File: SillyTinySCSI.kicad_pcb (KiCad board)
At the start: 4 copper layers, 53.5 x 25 mm, 53 parts, among them J301 Micro_SD_Card_Det1, J302 DB25_Plug, U1 Pico W, U101 74LVT125, U102 74LVT125, U105 74LVT245, U106 74LVT245, U301 MIC5219-2.85YM5

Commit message: fix BOM and proposed RTM files
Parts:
- added D304: LED, LED_SMD:LED_0805_2012Metric, F.Cu at (159.3, 51.7)
- R304: value 62 -> 51
- RN301, RN302: value 110 -> 120
- moved D302 0.32 mm to (159.3, 51.7)
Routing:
- net GND: track 110.3 -> 119.1 mm, vias 21 -> 24
- net Net-(D302-A): track 1.61 -> 9.69 mm, vias 0 -> 1
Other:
- board text added: "ZuluSCSI OSHW derivative by"
- board text removed: "${Brand} Pico OSHW derivative by"

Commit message: routing improvements
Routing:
- net +3V0: track 186.6 -> 199.2 mm
- net /cpu/SDIO_CLK: track 51.5 -> 47.1 mm
- net GND: track 119.1 -> 114.7 mm, vias 24 -> 25
- net /cpu/SDIO_D1: track 68.0 -> 63.8 mm
- net /cpu/SDIO_D3: track 66.7 -> 64.8 mm
- net /cpu/SDIO_D2: track 65.3 -> 63.4 mm
- net /cpu/SDIO_D0: track 61.0 -> 60.2 mm
- net +5V: track 59.5 -> 60.0 mm

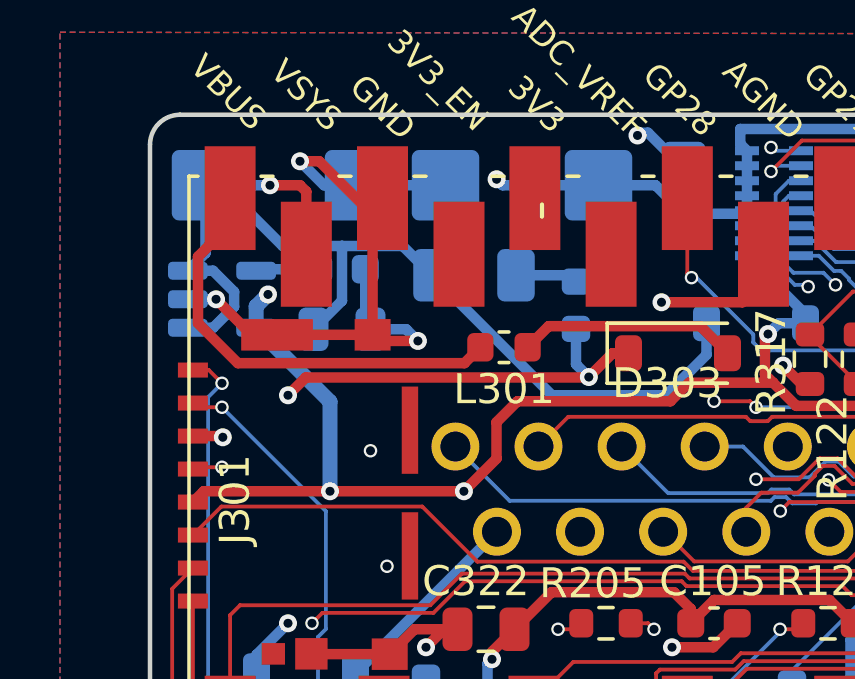
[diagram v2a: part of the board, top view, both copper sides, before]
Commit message: update regulator for manufacturing
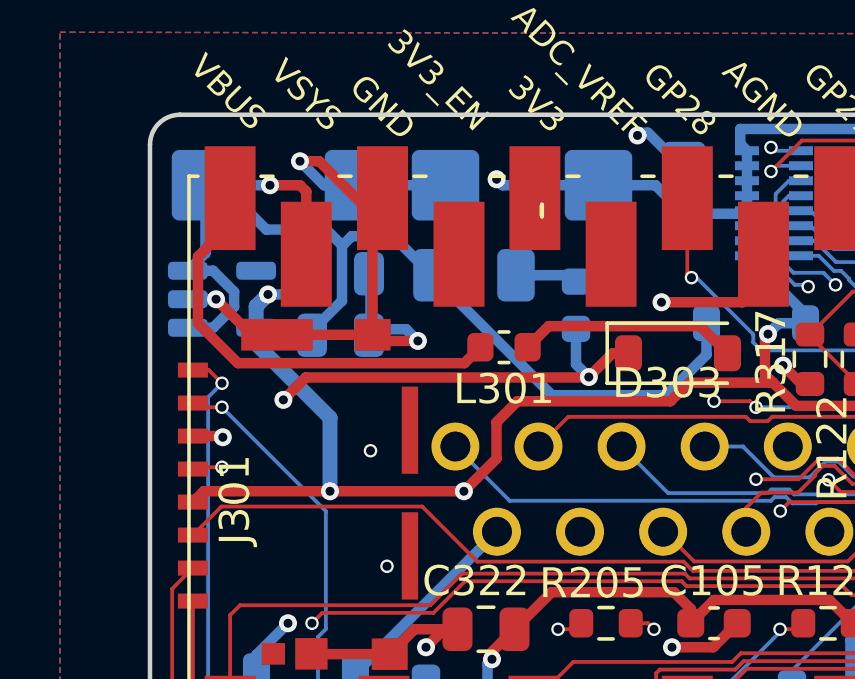
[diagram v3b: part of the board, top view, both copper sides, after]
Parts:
- removed C209: 470pf, Capacitor_SMD:C_0603_1608Metric
- added C305: 10uF, Capacitor_SMD:C_0805_2012Metric, B.Cu at (114.3, 55.5)
- U301: value MIC5219-2.85YM5 -> TLV75728PDBVR
- moved C301 0.21 mm to (114.3, 57.6)
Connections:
- U301 pad 4: Net-(U301-BP) -> unconnected-(U301-BP-Pad4)
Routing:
- net Net-(U301-BP): track 2.04 -> 0.00 mm
- net +3V0: track 199.2 -> 201.0 mm
